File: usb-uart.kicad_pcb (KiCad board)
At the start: 2 copper layers, 43.5 x 28.5 mm, 22 parts, among them CN1 USB4110-GF-A, CN2 30310-5002HB, SW1 CUS-12B, U1 PRTR5V0U2X, U2 FT231XQ

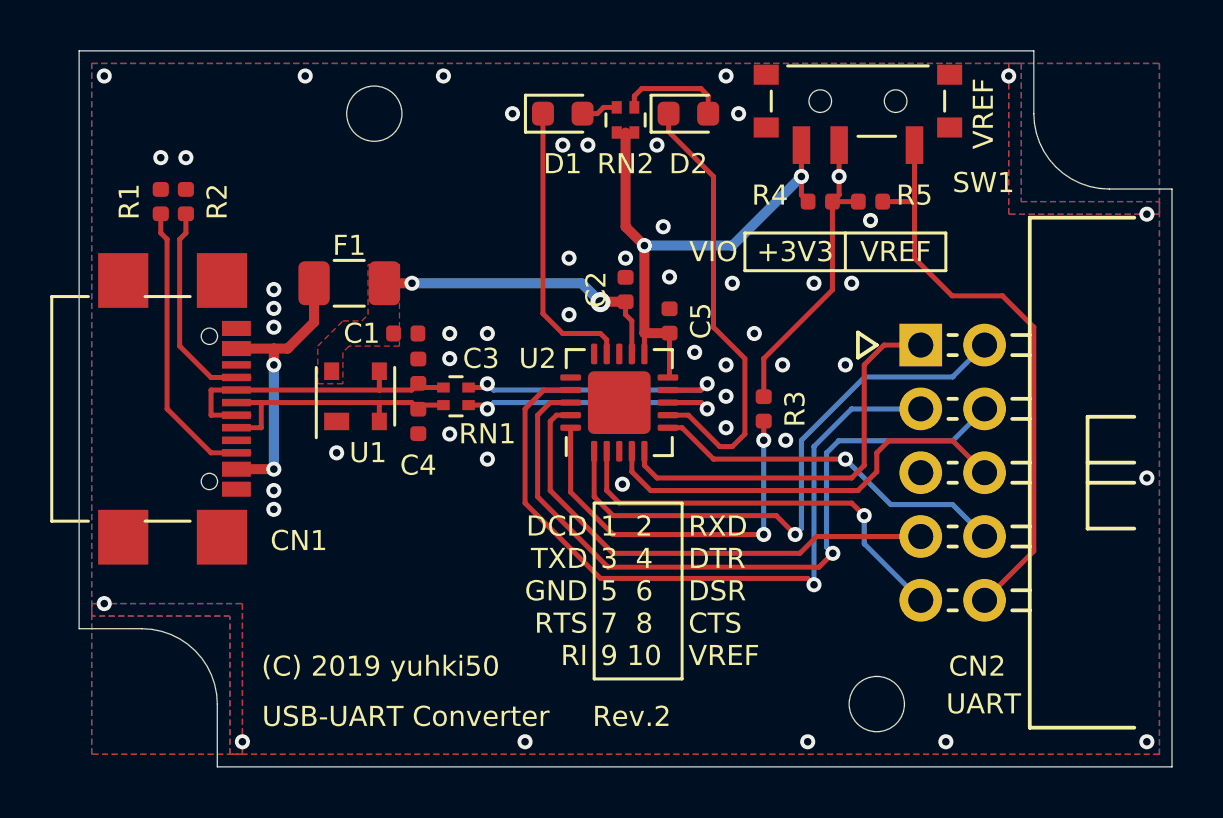
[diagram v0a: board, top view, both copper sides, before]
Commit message: update for new kicad
opened files in kicad 7 and saved. Plans to modify for USB type c and automatic boot control of esp32 via DTR/RTS mosfet on EN/GPIO0
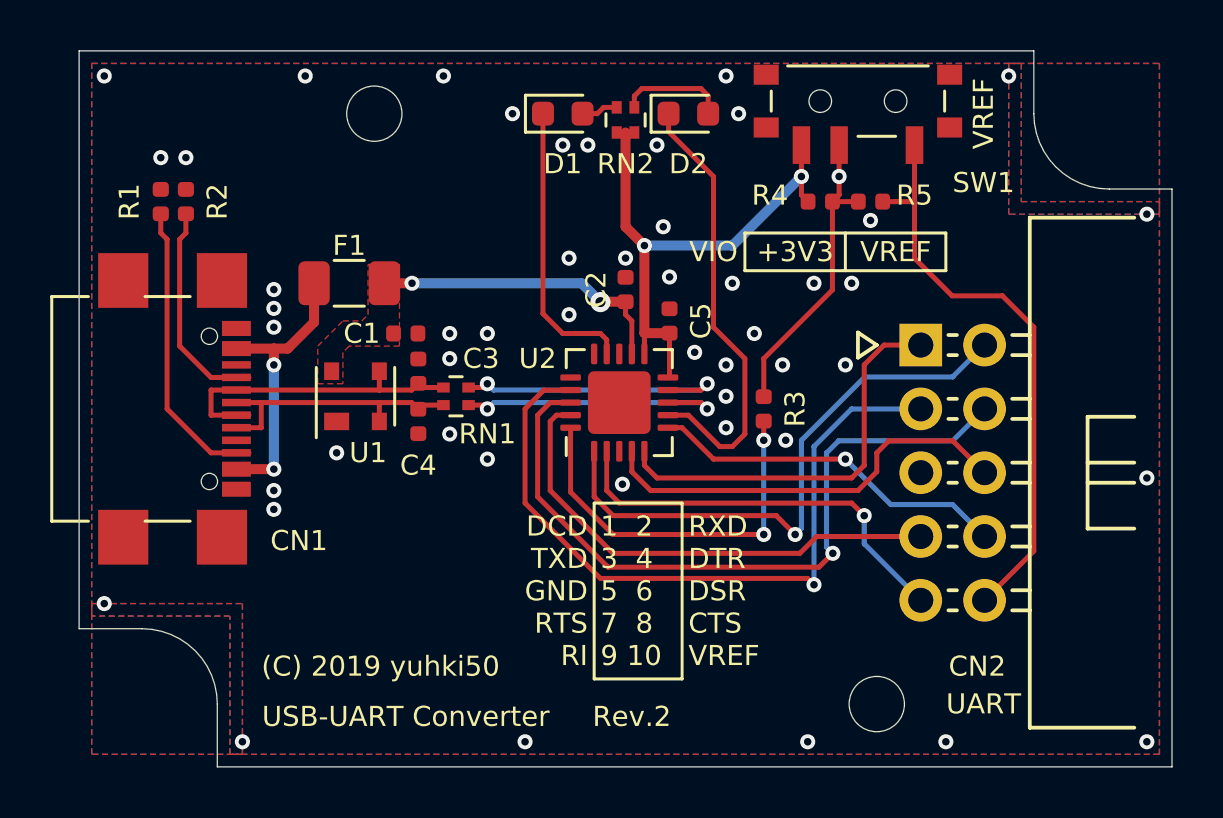
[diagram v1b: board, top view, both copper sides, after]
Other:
- net class Default removed
